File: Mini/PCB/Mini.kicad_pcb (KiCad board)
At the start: 2 copper layers, 155.9 x 99.3 mm, 30 parts

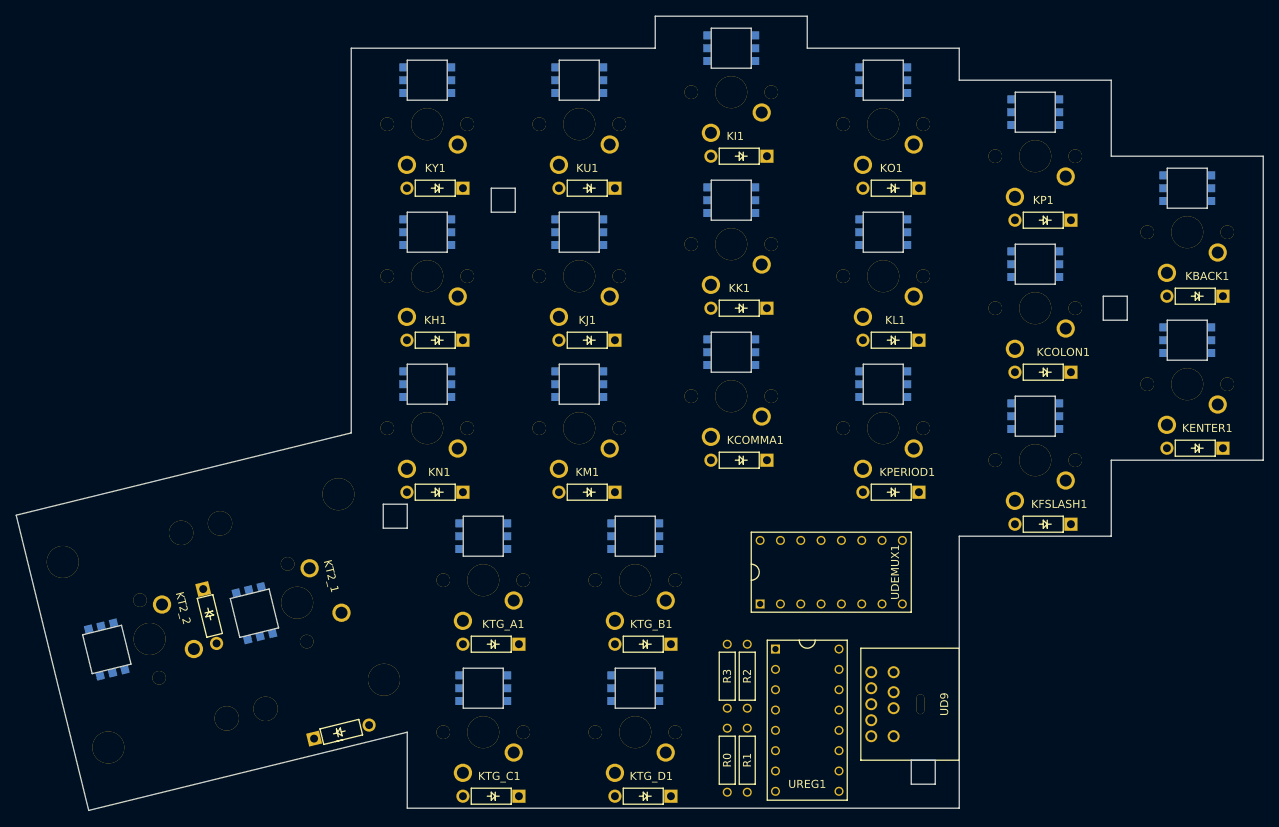
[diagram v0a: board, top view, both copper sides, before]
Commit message: Wiring diodes.
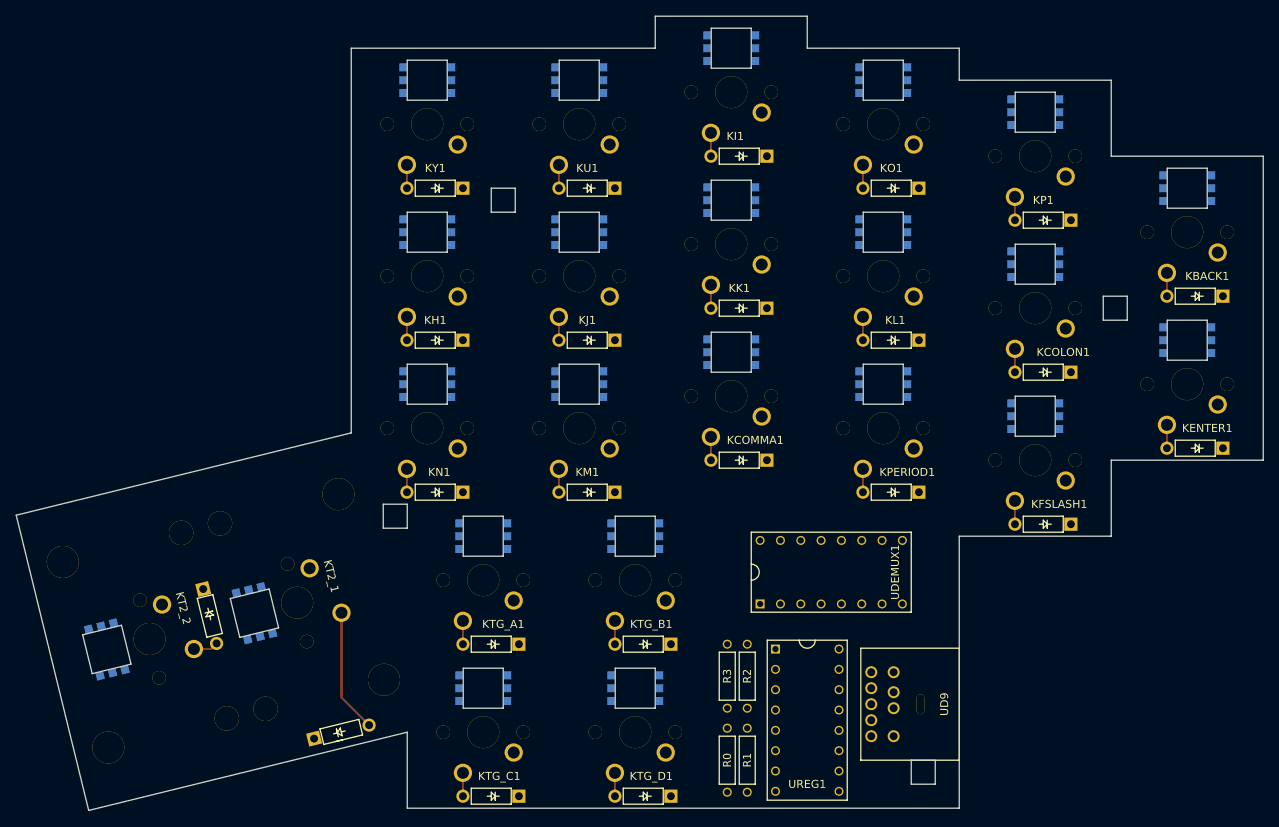
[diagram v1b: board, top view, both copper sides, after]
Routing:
- net Net-(KT2_1-Pad2): track 0.00 -> 15.5 mm
- net Net-(KT2_2-Pad2): track 0.00 -> 3.12 mm
- net Net-(KY1-Pad2): track 0.00 -> 2.92 mm
- net Net-(KU1-Pad2): track 0.00 -> 2.92 mm
- net Net-(KTG_D1-Pad2): track 0.00 -> 2.92 mm
- net Net-(KTG_C1-Pad2): track 0.00 -> 2.92 mm
- net Net-(KTG_B1-Pad2): track 0.00 -> 2.92 mm
- net Net-(KTG_A1-Pad2): track 0.00 -> 2.92 mm
- net Net-(KSEMICOLON1-Pad2): track 0.00 -> 2.92 mm
- net Net-(KPERIOD1-Pad2): track 0.00 -> 2.92 mm
- net Net-(KP1-Pad2): track 0.00 -> 2.92 mm
- net Net-(KO1-Pad2): track 0.00 -> 2.92 mm
- net Net-(KN1-Pad2): track 0.00 -> 2.92 mm
- net Net-(KM1-Pad2): track 0.00 -> 2.92 mm
- net Net-(KL1-Pad2): track 0.00 -> 2.92 mm
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
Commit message: Adding a bunch of wiring.
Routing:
- net C0: track 0.00 -> 111.1 mm
- net C1: track 0.00 -> 107.5 mm
- net C2: track 0.00 -> 84.6 mm
- net C3: track 0.00 -> 70.3 mm
- net VCC: track 0.00 -> 64.2 mm
- net GND: track 0.00 -> 50.4 mm
- net S0_DL: track 0.00 -> 22.5 mm, vias 0 -> 1
- net Net-(KENTER1-Pad9): track 0.00 -> 18.1 mm
- net S1: track 0.00 -> 17.9 mm, vias 0 -> 1
- net RX: track 0.00 -> 17.5 mm
- net S2: track 0.00 -> 17.4 mm, vias 0 -> 1
- net Net-(KENTER1-Pad10): track 0.00 -> 16.9 mm
- net Net-(KBACKSPACE1-Pad7): track 0.00 -> 16.9 mm
- net Net-(KBACKSPACE1-Pad6): track 0.00 -> 16.9 mm
- net SH_LD: track 0.00 -> 14.8 mm
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
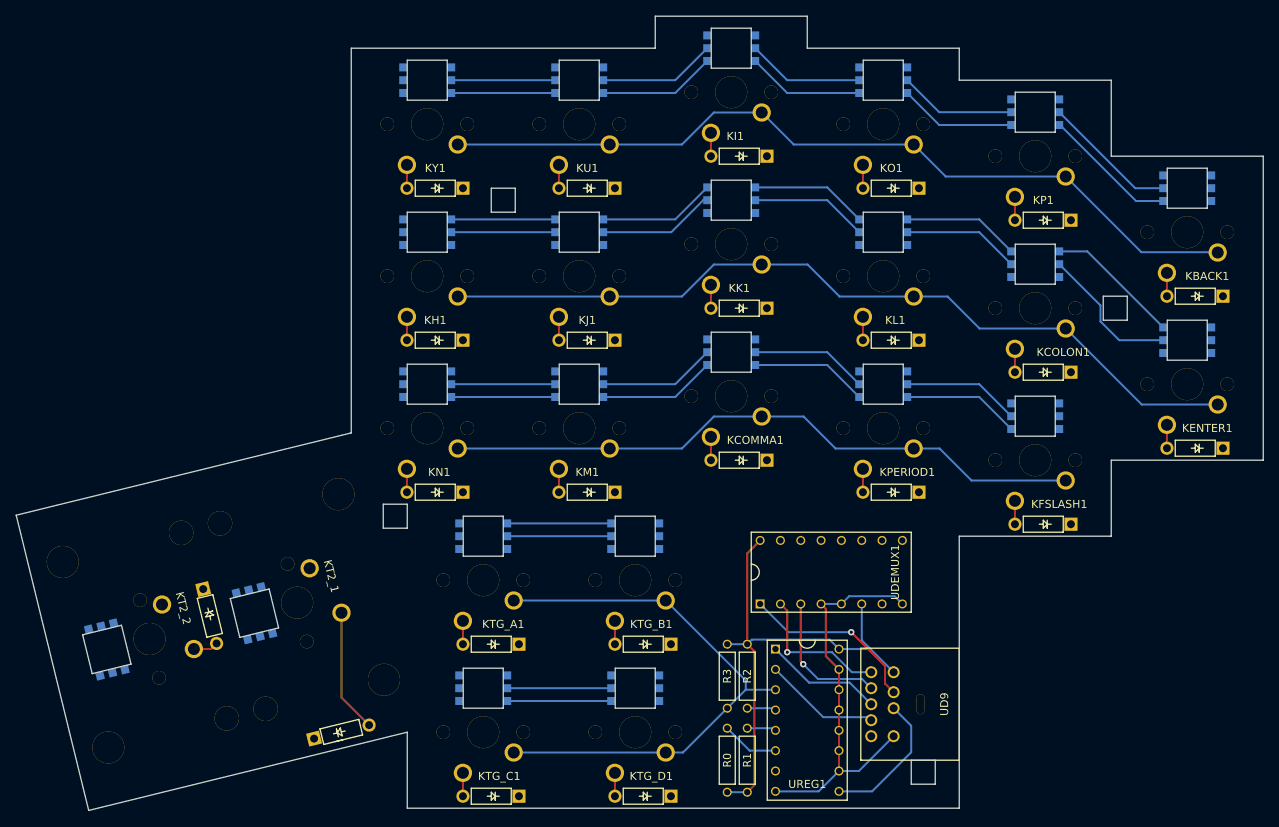
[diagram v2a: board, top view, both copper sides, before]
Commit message: Wiring everything except LED VCC/GND.
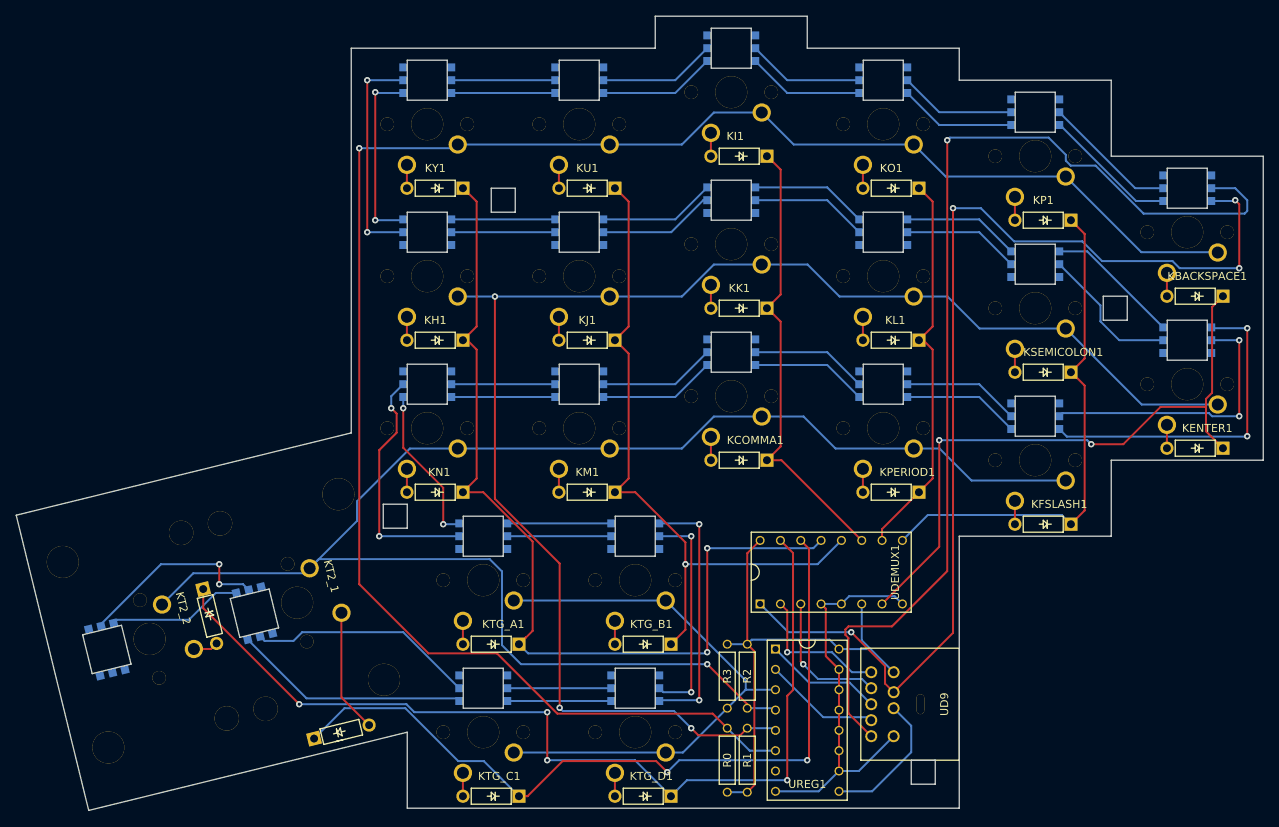
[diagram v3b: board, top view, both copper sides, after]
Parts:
- renumbered KBACK1 to KBACKSPACE1, KCOLON1 to KSEMICOLON1
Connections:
- KL1 pad 4: Net-(KL1-Pad4) -> R5
- KO1 pad 4: Net-(KL1-Pad4) -> R5
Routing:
- net CLK_L: track 0.00 -> 132.9 mm, vias 0 -> 1
- net C0: track 111.1 -> 231.6 mm, vias 0 -> 1
- net R0: track 0.00 -> 120.4 mm, vias 0 -> 4
- net R2: track 0.00 -> 117.7 mm, vias 0 -> 2
- net C2: track 84.6 -> 199.6 mm, vias 0 -> 1
- net S0_DL: track 22.5 -> 136.8 mm, vias 1 -> 4
- net R1: track 0.00 -> 98.8 mm, vias 0 -> 2
- net R3: track 0.00 -> 86.5 mm, vias 0 -> 1
- net C1: track 107.5 -> 187.6 mm, vias 0 -> 3
- net R7: track 0.00 -> 79.7 mm, vias 0 -> 2
- net R6: track 0.00 -> 63.7 mm
- net R4: track 0.00 -> 56.9 mm
- net R5: track 0.00 -> 49.7 mm
- net Net-(KENTER1-Pad7): track 0.00 -> 42.0 mm, vias 0 -> 2
- net Net-(KENTER1-Pad6): track 0.00 -> 35.8 mm, vias 0 -> 2
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
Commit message: Wiring up LED VCC.
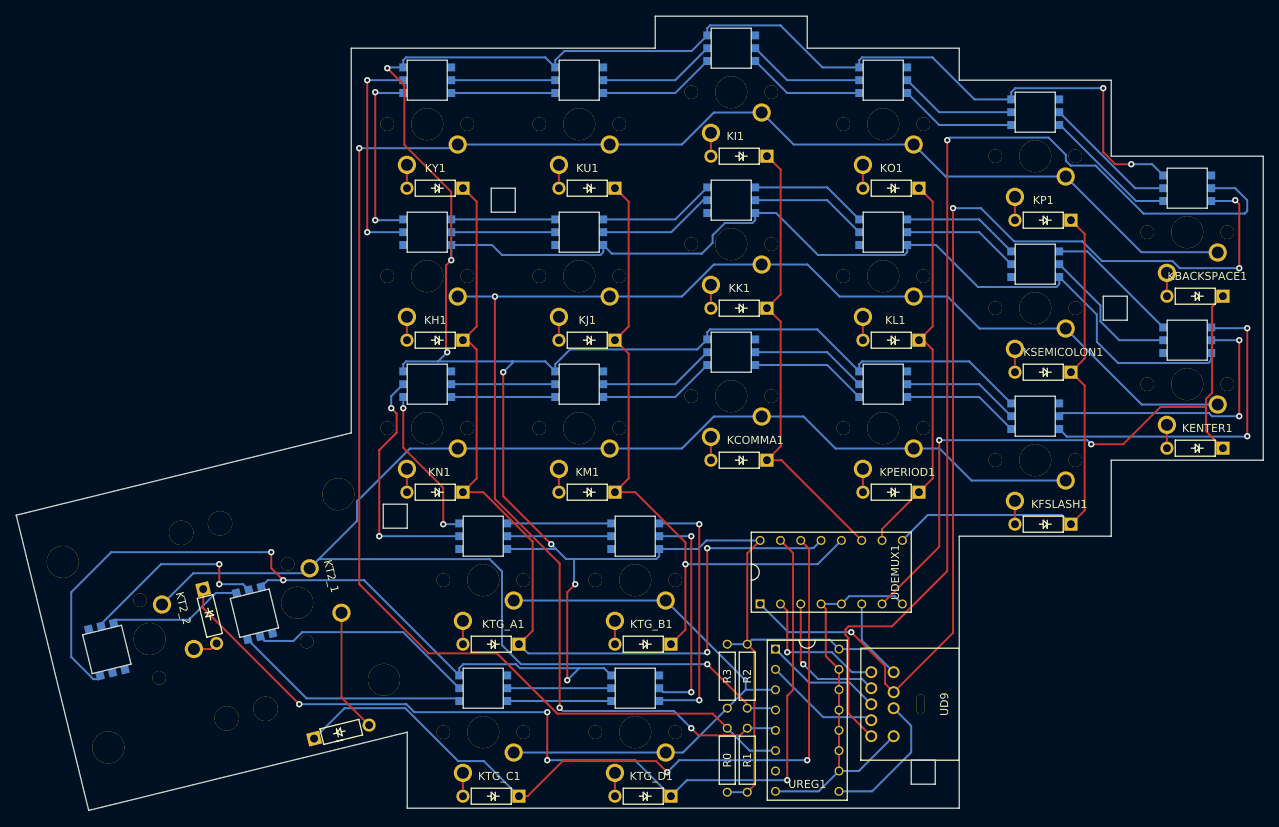
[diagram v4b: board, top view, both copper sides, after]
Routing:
- net VCC: track 64.2 -> 597.6 mm, vias 0 -> 11

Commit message: Generating gerber files and drill file.
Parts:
- renumbered KBACKSPACE1 to KBACK1, KSEMICOLON1 to KCOLON1
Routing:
- net GND: track 50.4 -> 631.1 mm, vias 0 -> 33
